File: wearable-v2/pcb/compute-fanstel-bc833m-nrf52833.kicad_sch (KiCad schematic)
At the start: 18 parts, among them J5 HERALD_V2_CONN_PLUG, U6 BC833, U7 MX25R6435F, U8 PCF85063ATL, Y1 32.768kHz

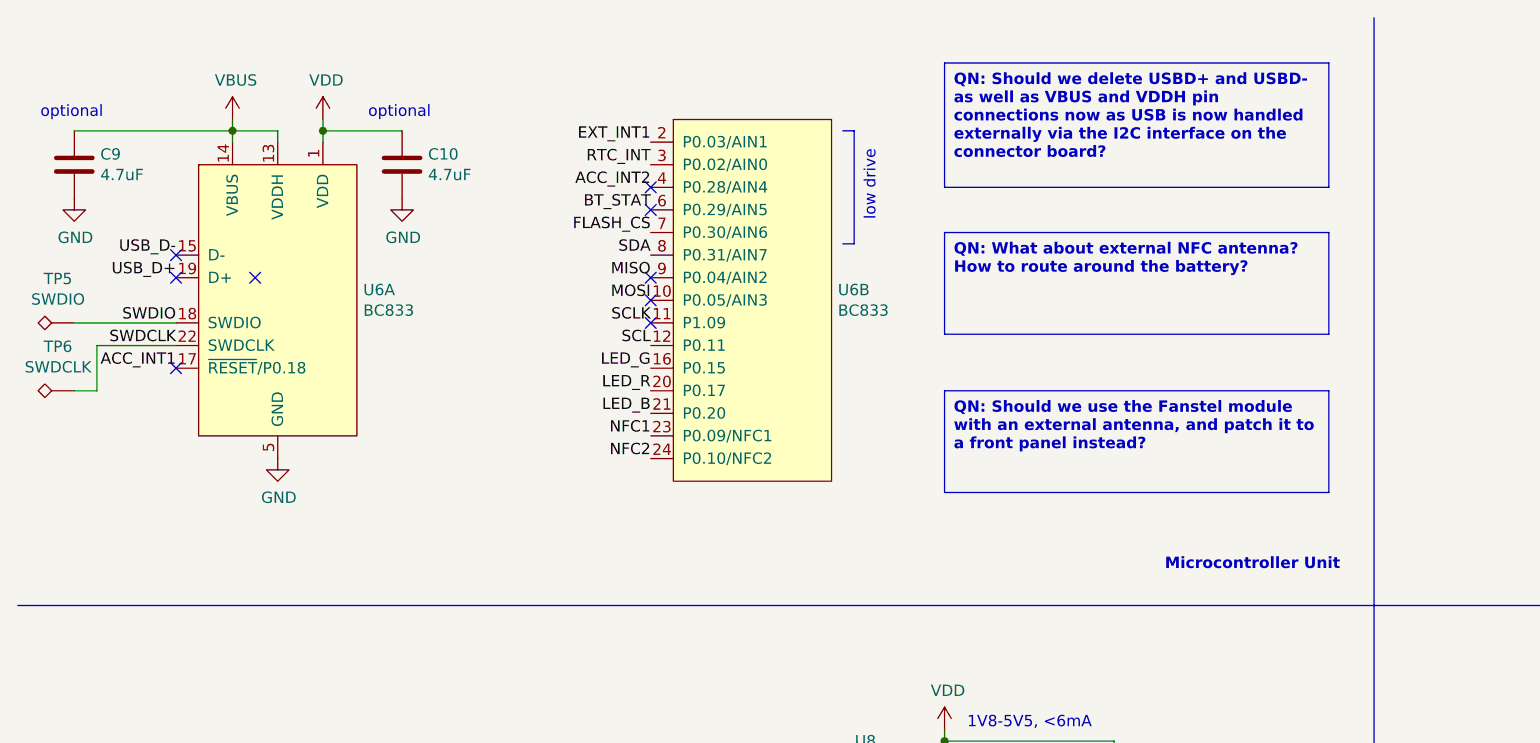
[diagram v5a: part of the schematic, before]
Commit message: Added I2C and I3C notes and additional resistors
Signed-off-by: Adam Fowler <adam@adamfowler.org>
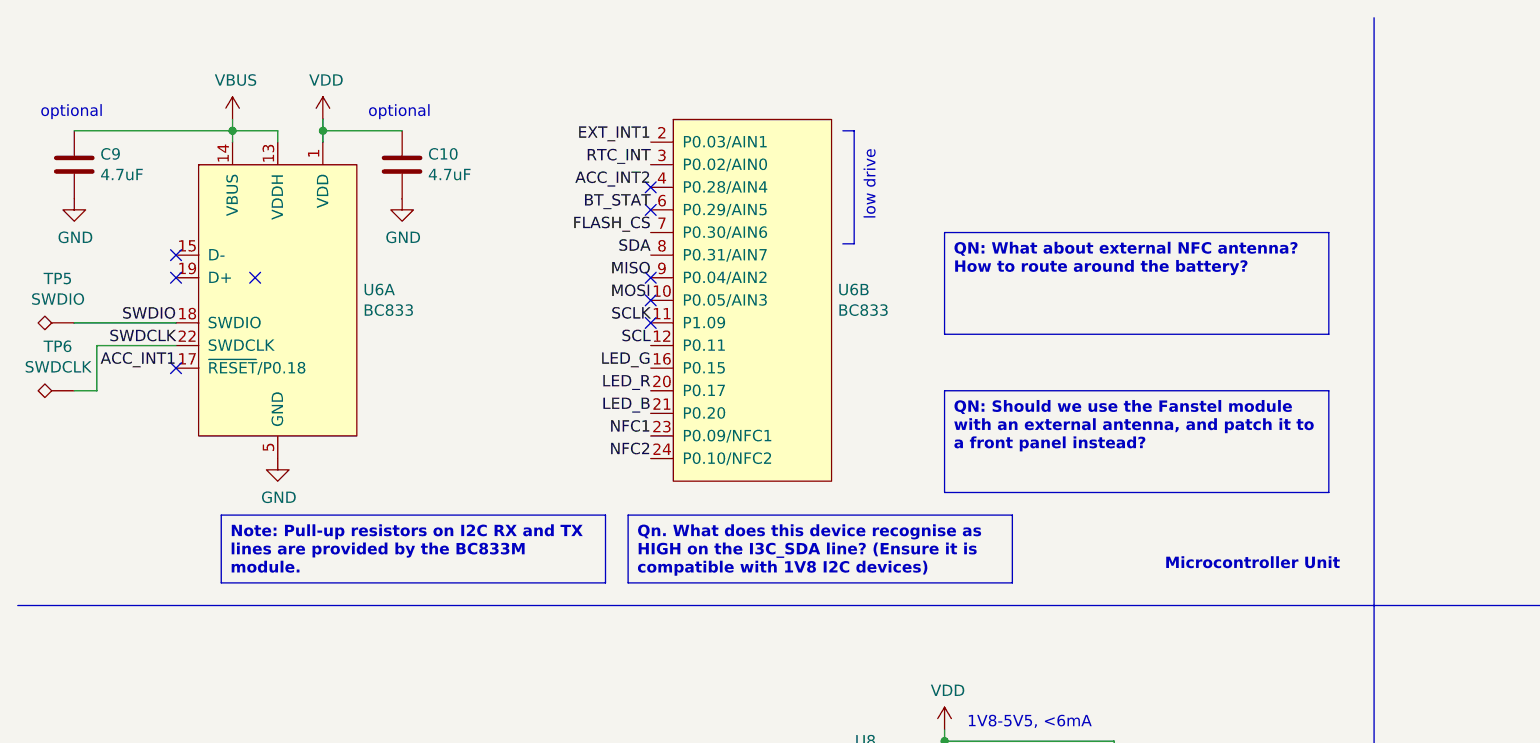
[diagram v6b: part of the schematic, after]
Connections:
- net USB_D+: no longer names the net of U6.19 (D+)
- net USB_D-: no longer names the net of U6.15 (D-)
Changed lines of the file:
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@@
     (effects (font (size 1.27 1.27) (thickness 0.254) bold) (justify left top))
   )
-  (text_box "QN: Should we delete USBD+ and USBD- as well as VBUS and VDDH pin connections now as USB is now handled externally via the I2C interface on the connector board?"
-    (at 118.11 17.78 0) (size 43.18 13.97)
+  (text_box "Note: Pull-up resistors on I2C RX and TX lines are provided by the BC833M module."
+    (at 36.83 68.58 0) (size 43.18 7.62)
     (stroke (width 0) (type default))
     (fill (type none))
@@
   (text_box "This 64Mbit chipd is bigger than the original 8Mbit one, but still low power. 512Mbit is available, but it uses approx 20x the power."
     (at 16.51 185.42 0) (size 46.99 8.89)
+    (stroke (width 0) (type default))
+    (fill (type none))
+    (effects (font (size 1.27 1.27) (thickness 0.254) bold) (justify left top))
+  )
+  (text_box "Qn. What does this device recognise as HIGH on the I3C_SDA line? (Ensure it is compatible with 1V8 I2C devices)"
+    (at 82.55 68.58 0) (size 43.18 7.62)
     (stroke (width 0) (type default))
     (fill (type none))
@@
     (effects (font (size 1.27 1.27)) (justify right bottom))
   )
-  (label "USB_D+" (at 31.75 41.91 180) (fields_autoplaced)
-    (effects (font (size 1.27 1.27)) (justify right bottom))
-  )
   (label "MOSI" (at 85.09 44.45 180) (fields_autoplaced)
     (effects (font (size 1.27 1.27)) (justify right bottom))
@@
     (effects (font (size 1.27 1.27)) (justify right bottom))
   )
-  (label "USB_D-" (at 31.75 39.37 180) (fields_autoplaced)
-    (effects (font (size 1.27 1.27)) (justify right bottom))
-  )
